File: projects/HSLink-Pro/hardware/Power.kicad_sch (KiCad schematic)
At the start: 44 parts, among them U1 HPM5301IEG1, U10 EA3036C, U13 LMV321

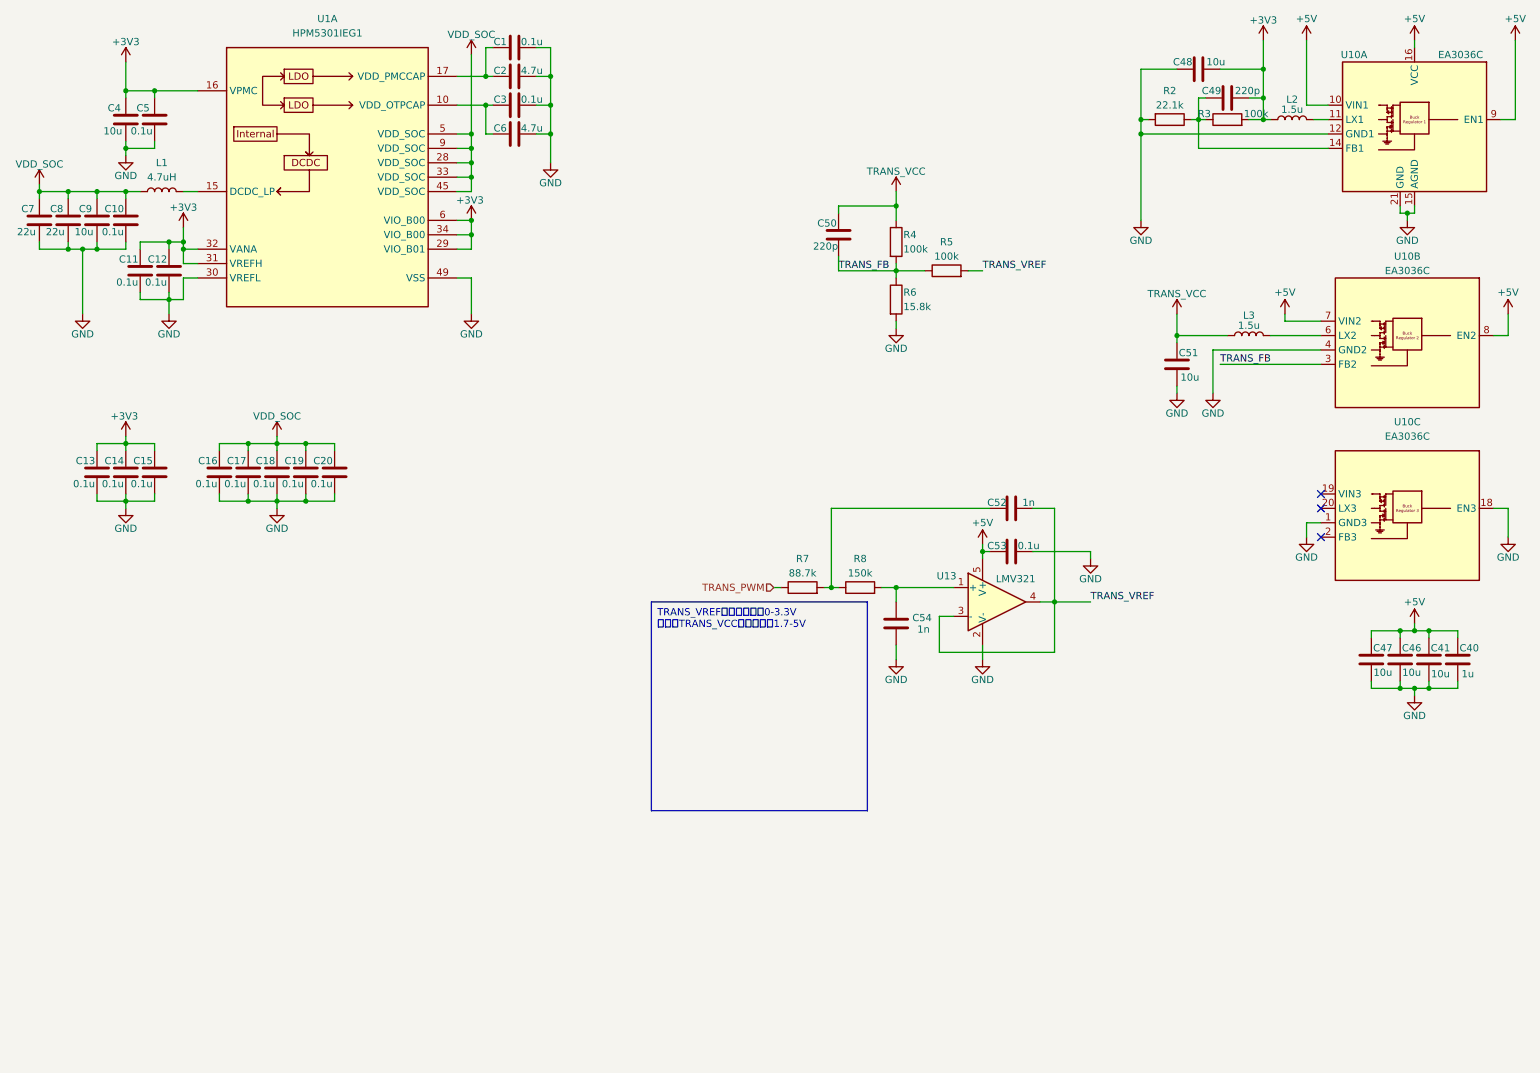
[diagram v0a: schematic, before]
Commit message: HSLink-Pro: 2.3.1 (#29)
* update: 更新电源部分

* update: 更新原理图

* update: 更新PCB

- 修改定位孔位置
- 修改Type-C位置

* update: 添加RTT LOGO

* chore: 添加cJSON库

* feat: 添加与上位机的HID通信接口

* refactor: 重构命令解析部分代码

* fix: 修复描述符错误

* feat: 添加上位机下发设置功能

* feat: 添加数据保存

* fix: 修复可能的一些错误

* fix: 修复写入flash死机问题

* fix: 潜在的内存泄露问题

* chore: 添加tlsf

* chore: 切换cJSON库位置

* feat: 内存管理切换为tlsf

* feat: 添加首次默认设置

* feat: 添加硬件版本号

* feat: 添加获取设置

* chore: 将项目修改为cpp

* feat: 重构为cpp

* fix: 修复release下可能会崩溃的玄学问题

* chore: 删除cJSON库

* fix: 修复RapidJSON库所需内存

* fix: 修复nickname设置问题

* fix: BL工程编译失败

* fix: BL工程里面关闭所有输出

* fix: 修复一些warning

* update: README

* fix: get_setting字段错误

* update: 1.2.0硬件

* style: 统一接口命名

* feat: 添加upgrade命令

* fix: 将硬件版本号放在OTP寄存器中

* fix: 解决初始值问题

* fix: PWM输出极性反了

* fix: 1.2.0硬件修改IO

* release: 2.3.1
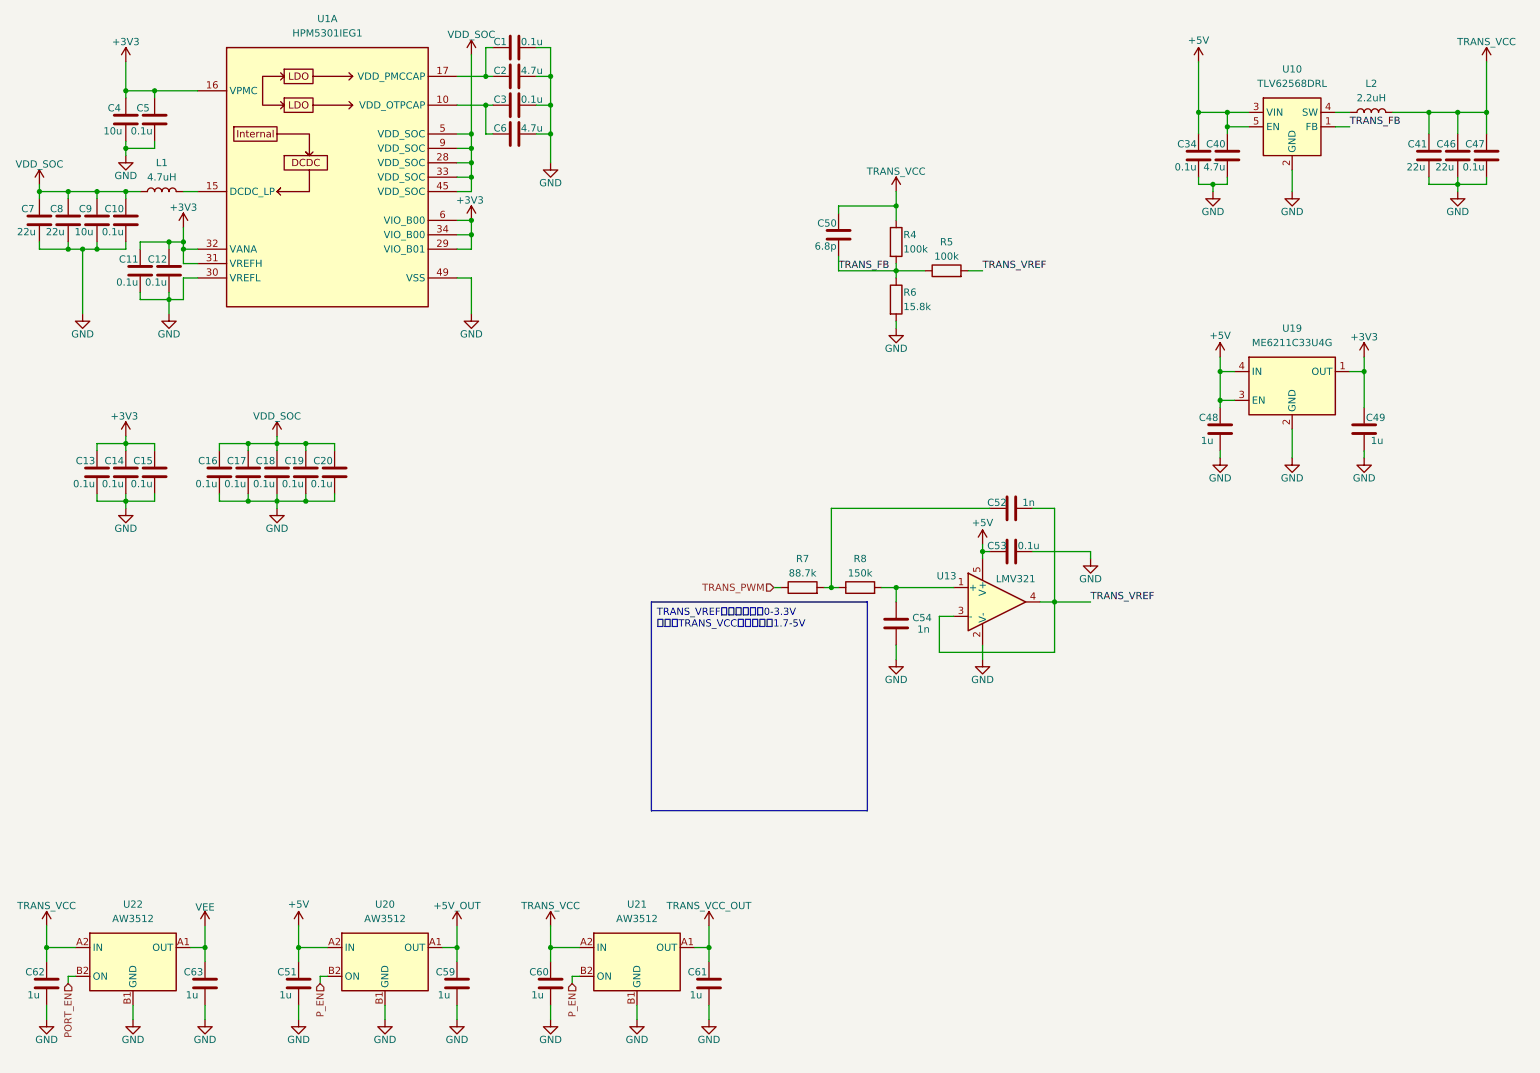
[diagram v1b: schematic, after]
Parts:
- removed L3: 1.5u, Inductor_SMD:L_1008_2520Metric, symbol Device:L
- removed R2: 22.1k, Resistor_SMD:R_0402_1005Metric, symbol Device:R
- removed R3: 100k, Resistor_SMD:R_0402_1005Metric, symbol Device:R
- removed U10: EA3036C, Package_DFN_QFN:QFN-20-1EP_3x3mm_P0.4mm_EP1.65x1.65mm, symbol Regulator_Switching:EA3036C
- added C34: 0.1u, Capacitor_SMD:C_0402_1005Metric, symbol Device:C
- added C59, C60, C61, C62, C63: 1u, Capacitor_SMD:C_0402_1005Metric, symbol Device:C
- added U10: TLV62568DRL, Package_TO_SOT_SMD:SOT-563, symbol Regulator_Switching:TLV62568DRL
- added U19: ME6211C33U4G, Package_DFN_QFN:OnSemi_XDFN4-1EP_1.0x1.0mm_EP0.52x0.52mm, symbol Regulator_Linear:NCP115AMX120TCG
- added U20, U21, U22: AW3512, Package_CSP:WLCSP-4-X1-WLB0909-4_0.89x0.89mm_P0.5mm, symbol Power_Management:AP22913CN4
- C40: value 1u -> 4.7u
- C41, C46: value 10u -> 22u
- C47: value 10u -> 0.1u; footprint Capacitor_SMD:C_0603_1608Metric -> Capacitor_SMD:C_0402_1005Metric
- C48: value 10u -> 1u
- C49: value 220p -> 1u
- C50: value 220p -> 6.8p
- C51: value 10u -> 1u; footprint Capacitor_SMD:C_0603_1608Metric -> Capacitor_SMD:C_0402_1005Metric
- L1: footprint Inductor_SMD:L_1008_2520Metric -> Inductor_SMD:L_Murata_DFE201610P
- L2: value 1.5u -> 2.2uH; footprint Inductor_SMD:L_1008_2520Metric -> Inductor_SMD:L_Murata_DFE201610P
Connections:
- net +3V3: now also C49.1, U19.1 (OUT); no longer C48.2, C49.2, L2.1
- net +5V: now also C48.1, C51.1, C34.1, U10.3 (VIN), U10.5 (EN), U19.3 (EN), U19.4 (IN), U20.A2 (IN); no longer C41.1, C46.1, C47.1
- net GND: now also C48.2, C49.2, C34.2, C59.2, C60.2, C61.2, C62.2, C63.2, U10.2 (GND), U19.2 (GND), U19.5 (GND), U20.B1 (GND), U21.B1 (GND), U22.B1 (GND); no longer C48.1
- net TRANS_FB: now also U10.1 (FB)
- net TRANS_VCC: now also C41.1, C46.1, C47.1, L2.2, C60.1, C62.1, U21.A2 (IN), U22.A2 (IN); no longer C51.1
- new net: L2.1, U10.4 (SW)
- new net +5V_OUT: C59.1, U20.A1 (OUT)
- new net PORT_EN: U22.B2 (ON)
- new net P_EN: U20.B2 (ON), U21.B2 (ON)
- new net TRANS_VCC_OUT: C61.1, U21.A1 (OUT)
- new net VEE: C63.1, U22.A1 (OUT)
- no-connect marks 3 -> 0

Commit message: update: hardware 1.2.1
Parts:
- removed U19: ME6211C33U4G, Package_DFN_QFN:OnSemi_XDFN4-1EP_1.0x1.0mm_EP0.52x0.52mm, symbol Regulator_Linear:NCP115AMX120TCG
- removed U20, U21, U22: AW3512, Package_CSP:WLCSP-4-X1-WLB0909-4_0.89x0.89mm_P0.5mm, symbol Power_Management:AP22913CN4
- added U19: ME6211C33R5, Package_TO_SOT_SMD:SOT-353_SC-70-5, symbol Regulator_Linear:ME6211C33M5
- added U21, U22, U7: TPS22965, Package_SON:WSON-8-1EP_2x2mm_P0.5mm_EP0.9x1.6mm, symbol Load Switch:TPS22965
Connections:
- net +3V3: now also U19.5 (V_{OUT})
- net +5V: now also U19.1 (V_{IN}), U19.3 (CE), U22.1 (V_{IN}), U22.2 (V_{IN}), U22.4 (VBIAS)
- net +5V_OUT: now also U22.7 (V_{OUT}), U22.8 (V_{OUT})
- net PORT_EN: now also U7.3 (ON)
- net P_EN: now also U21.3 (ON), U22.3 (ON)
- net TRANS_VCC: now also U21.1 (V_{IN}), U21.2 (V_{IN}), U21.4 (VBIAS), U7.1 (V_{IN}), U7.2 (V_{IN}), U7.4 (VBIAS)
- net TRANS_VCC_OUT: now also U21.7 (V_{OUT}), U21.8 (V_{OUT})
- net VEE: now also U7.7 (V_{OUT}), U7.8 (V_{OUT})
- net GND renamed EP
- net EP: now also U19.2 (V_{SS}), U21.5 (GND), U21.9 (EP), U22.5 (GND), U22.9 (EP), U7.5 (GND), U7.9 (EP)
- no-connect marks 0 -> 3
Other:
- moved on the sheet: C51
